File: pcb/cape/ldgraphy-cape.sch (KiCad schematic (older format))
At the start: 22 parts, among them P1 12V, P2 Laser, P3 Jumper, P4 Stepper, P5 CONN_01X05, P6 12V-in, P7 5V-in, P8 BB_P8, P9 BB_P9, Q1 BC237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

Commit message: o Update cape: include hsync circuit o Laser driver: new board that uses the new OpAmp circuit   (not tested yet)
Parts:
- removed C1: 100n, Capacitors_SMD:C_0805, symbol C
- removed C2: 10u, Capacitors_SMD:C_1206, symbol C
- removed P1: 12V, Pin_Headers:Pin_Header_Straight_1x02, symbol CONN_01X02
- removed P4: Stepper, Pin_Headers:Pin_Header_Straight_1x04, symbol CONN_01X04
- removed Q1: BC237, TO_SOT_Packages_THT:TO-92_Molded_Narrow_Reverse, symbol BC237
- removed Q2: BD135, TO_SOT_Packages_THT:SOT126_SOT32_Housing_Horizontal, symbol BD135
- removed Q3: MTM232270, TO_SOT_Packages_SMD:SOT-323, symbol Q_NMOS_GSD
- removed R1: R, Resistors_ThroughHole:Resistor_Horizontal_RM15mm, symbol R
- removed R2, R3: R, Capacitors_SMD:C_0603, symbol R
- removed R4: 100, Resistors_SMD:R_0603, symbol R
- removed R5: 4R7, Resistors_ThroughHole:Resistor_Horizontal_RM15mm, symbol R
- removed R6: 470, Resistors_ThroughHole:Resistor_Horizontal_RM15mm, symbol R
- removed RV1: POT, Potentiometers:Potentiometer_WirePads_Small, symbol POT
- added C10: C, Capacitors_SMD:C_0603, symbol C
- added P4: CONN_02X04, Pin_Headers:Pin_Header_Straight_2x04_Pitch2.54mm_SMD, symbol CONN_02X04
- added R10, R11, R13, R14, R15, R9: R, Resistors_SMD:R_0603, symbol R
- added R12: 1k, Resistors_SMD:R_0603, symbol R
- added R16: 2k2, Resistors_SMD:R_0603, symbol R
- added TP4: HSync, Measurement_Points:Measurement_Point_Round-SMD-Pad_Small, symbol TEST_1P
- added TP5: VPhoto, Measurement_Points:Measurement_Point_Round-SMD-Pad_Small, symbol TEST_1P
- added U3, U4: MIC920, TO_SOT_Packages_SMD:SOT-353_SC-70-5, symbol MIC920
- P2: value Laser -> PhDiode; footprint Pin_Headers:Pin_Header_Straight_1x02 -> Pin_Headers:Pin_Header_Straight_2x01_Pitch2.54mm
- P3: footprint (none) -> Pin_Headers:Pin_Header_Straight_2x03_Pitch2.54mm_SMD
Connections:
- net labels added: HSyncTrig, Hsync, VPhoto, ~MOTORS_EN
- net labels removed: ~SLED_EN
- wire segments 56 -> 66
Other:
- note added: "A"
- note added: "K"
- note added: "Photo Diode Amp"
- note added: "Schmitt Trigger"
- note removed: "Keep laser lasing at\nlow level when "off"."
- note removed: "≈1.2V"
- note removed: "≈1.9V"
- moved on the sheet: P3, P5, P6, P7, U1

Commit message: o Sketch out cape. NB: different GPIO assignment than   current software expects.
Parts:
- removed P8: BB_P8, Pin_Headers:Pin_Header_Straight_2x23, symbol CONN_02X32
- added J1: CONN_01X03, Pin_Headers:Pin_Header_Straight_1x03_Pitch2.54mm, symbol CONN_01X03
- added R1: 4k7, Resistors_SMD:R_0603, symbol R
- added R2, R3, R4: 1k, Resistors_SMD:R_0603, symbol R
- P4: value CONN_02X04 -> BaseConn; footprint Pin_Headers:Pin_Header_Straight_2x04_Pitch2.54mm_SMD -> Pin_Headers:Pin_Header_Straight_2x05_Pitch2.54mm_SMD; symbol CONN_02X04 -> CONN_02X05
- P9: footprint Pin_Headers:Pin_Header_Straight_2x23 -> Pin_Headers:Pin_Header_Straight_2x18_Pitch2.54mm; symbol CONN_02X32 -> CONN_02X23
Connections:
- net +12V: now also J1.1 (P1)
- net 3.3V: now also R1.1, R2.2, R3.2, R4.2
- net GND: now also P4.5 (P5), P4.6 (P6), J1.3 (P3); no longer P4.3 (P3), P4.4 (P4)
- net Hsync: now also P9.23 (P23), R12.1, R16.2; no longer P9.11 (P11)
- net LASER_DATA: now also J1.2 (P2)
- net SLED_DIR: now also P9.14 (P14); no longer P9.15 (P15)
- net SLED_STEP: now also P9.15 (P15); no longer P9.14 (P14)
- net ~MOTORS_EN: now also P9.16 (P16), R1.2; no longer P9.13 (P13)
- net ~StopBack: now reaches P9.12 (P12)
- net ~StopBack: now also P4.4 (P4), R4.1
- net at U1.11 (1B): now also P4.8 (P8); no longer P4.6 (P6)
- net at U1.12 (1A): now also P4.10 (P10); no longer P4.8 (P8)
- net at U1.13 (2A): now also P4.9 (P9); no longer P4.7 (P7)
- net at U1.14 (2B): now also P4.7 (P7); no longer P4.5 (P5)
- net ~UI-Button: now reaches P4.2 (P2)
- net ~UI-Button: now also P9.11 (P11), R3.1
- new net ~StopFront: P4.3 (P3), P9.13 (P13), R2.1

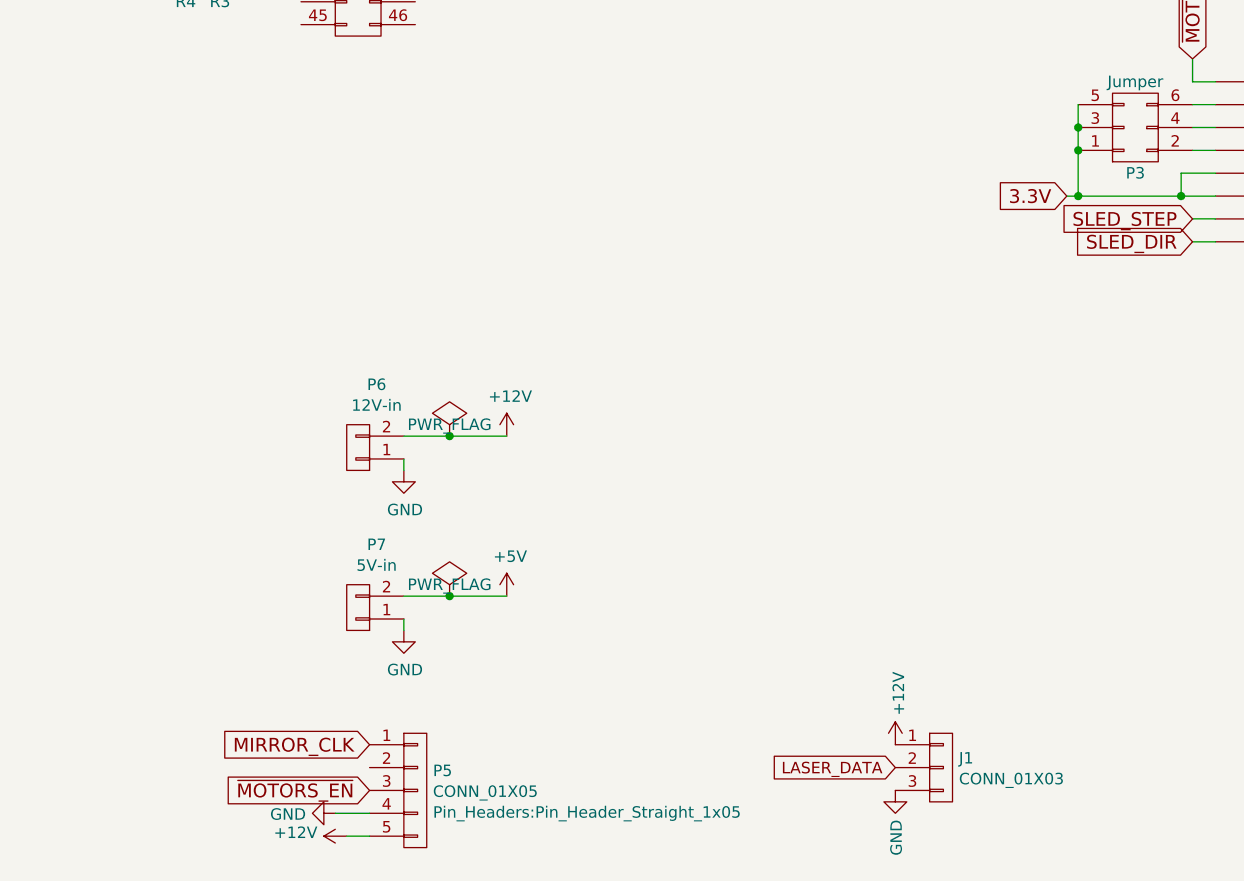
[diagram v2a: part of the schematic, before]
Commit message: o Add DC/DC converter to cape.
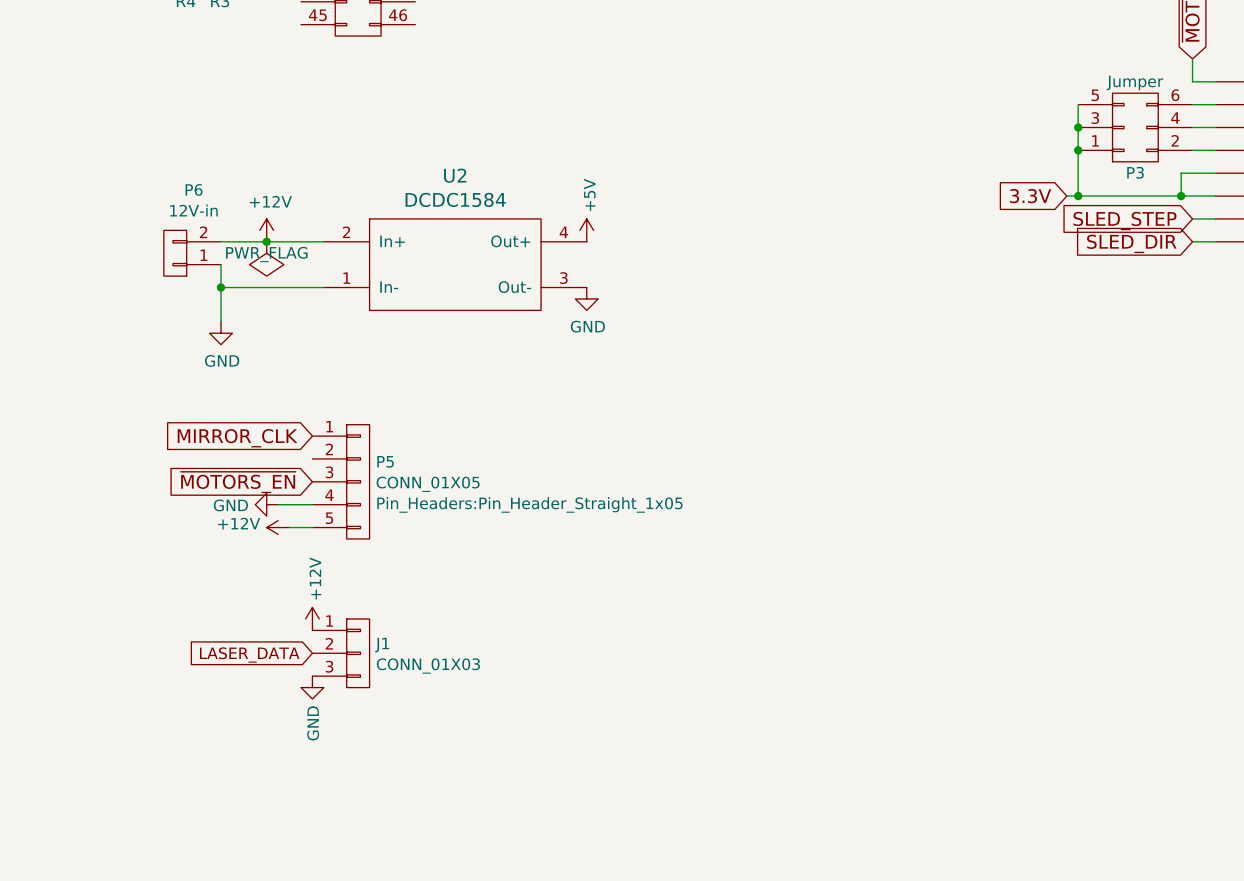
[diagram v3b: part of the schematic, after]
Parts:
- removed P7: 5V-in, symbol CONN_01X02
- added U2: DCDC1584, ldgraphy:dcdc-mp1584, symbol DCDC1584
- P6: footprint (none) -> Pin_Headers:Pin_Header_Straight_1x02_Pitch2.54mm
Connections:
- net +12V: now also U2.2 (In+)
- net +5V: now also U2.4 (Out+)
- net GND: now also U2.1 (In-), U2.3 (Out-)
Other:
- moved on the sheet: J1, P5, P6

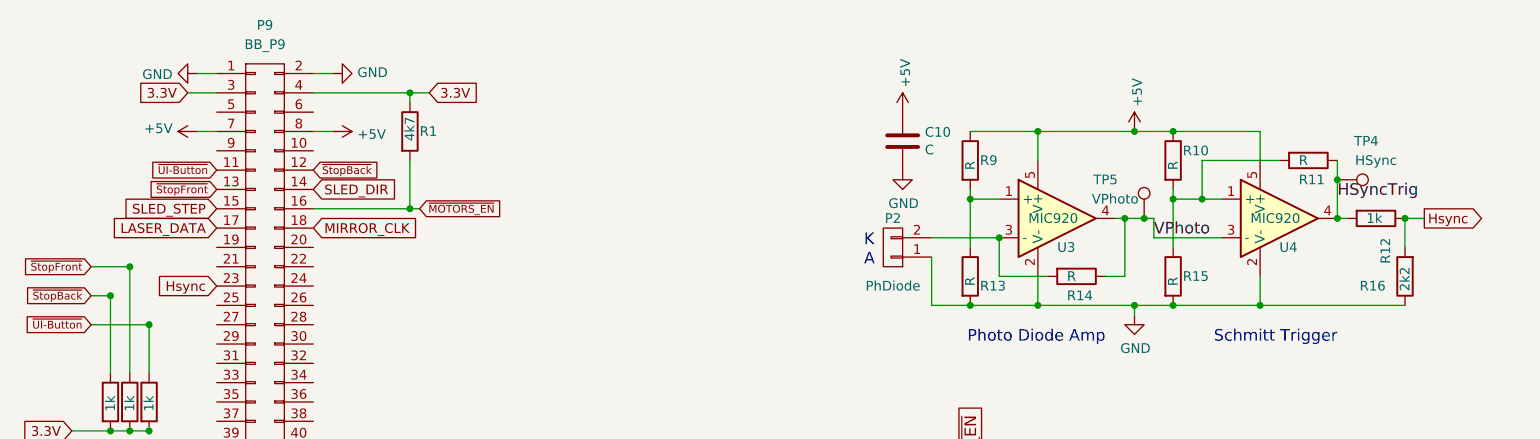
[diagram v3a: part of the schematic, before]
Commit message: o Update values in schematics.
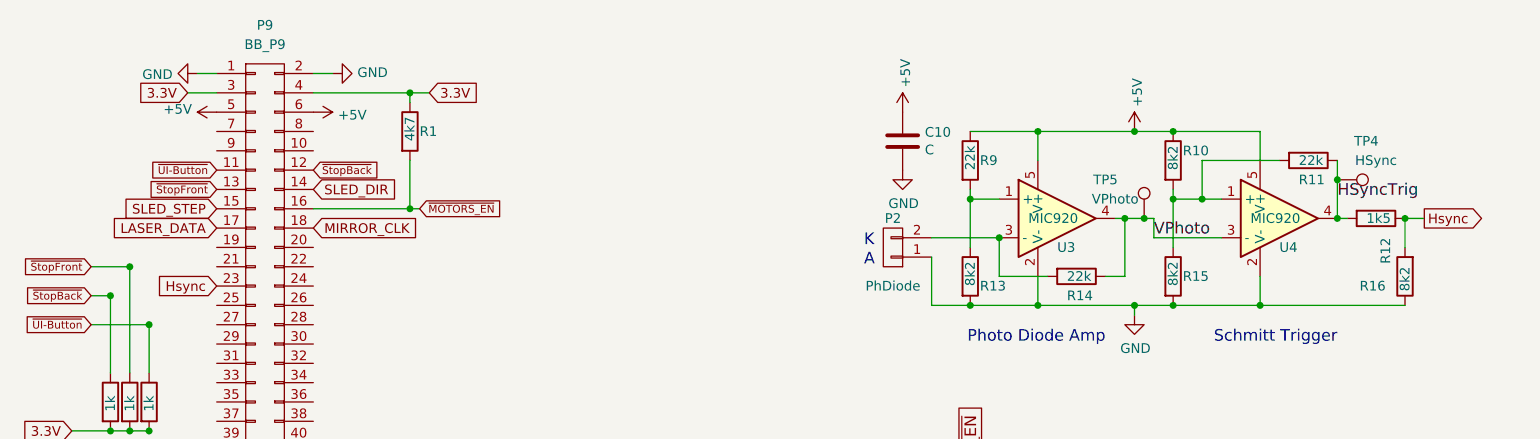
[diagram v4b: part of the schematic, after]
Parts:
- R10, R13, R15: value R -> 8k2
- R11, R14, R9: value R -> 22k
- R12: value 1k -> 1k5
- R16: value 2k2 -> 8k2
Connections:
- net +5V: now also P9.5 (P5), P9.6 (P6); no longer P9.7 (P7), P9.8 (P8)
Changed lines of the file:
@@
 L +5V #PWR5
 U 1 1 58741152
-P 2400 1350
-F 0 "#PWR5" H 2400 1200 50  0001 C CNN
-F 1 "+5V" V 2415 1478 50  0000 L CNN
-F 2 "" H 2400 1350 50  0000 C CNN
-F 3 "" H 2400 1350 50  0000 C CNN
-	1    2400 1350
+P 2300 1250
+F 0 "#PWR5" H 2300 1100 50  0001 C CNN
+F 1 "+5V" V 2315 1378 50  0000 L CNN
+F 2 "" H 2300 1250 50  0000 C CNN
+F 3 "" H 2300 1250 50  0000 C CNN
+	1    2300 1250
 	0    1    1    0
 $EndComp
@@
 L +5V #PWR4
 U 1 1 587412CA
-P 1700 1350
-F 0 "#PWR4" H 1700 1200 50  0001 C CNN
-F 1 "+5V" V 1715 1478 50  0000 L CNN
-F 2 "" H 1700 1350 50  0000 C CNN
-F 3 "" H 1700 1350 50  0000 C CNN
-	1    1700 1350
+P 1800 1250
+F 0 "#PWR4" H 1800 1100 50  0001 C CNN
+F 1 "+5V" V 1815 1378 50  0000 L CNN
+F 2 "" H 1800 1250 50  0000 C CNN
+F 3 "" H 1800 1250 50  0000 C CNN
+	1    1800 1250
 	0    -1   -1   0
 $EndComp
@@
 P 5700 1500
 F 0 "R9" H 5750 1500 50  0000 L CNN
-F 1 "R" V 5700 1450 50  0000 L CNN
+F 1 "22k" V 5700 1450 50  0000 L CNN
 F 2 "Resistors_SMD:R_0603" V 5630 1500 50  0001 C CNN
 F 3 "" H 5700 1500 50  0000 C CNN
@@
 P 5700 2100
 F 0 "R13" H 5750 2050 50  0000 L CNN
-F 1 "R" V 5700 2050 50  0000 L CNN
+F 1 "8k2" V 5700 2050 50  0000 L CNN
 F 2 "Resistors_SMD:R_0603" V 5630 2100 50  0001 C CNN
 F 3 "" H 5700 2100 50  0000 C CNN
@@
 P 6750 2100
 F 0 "R15" H 6800 2100 50  0000 L CNN
-F 1 "R" V 6750 2050 50  0000 L CNN
+F 1 "8k2" V 6750 2050 50  0000 L CNN
 F 2 "Resistors_SMD:R_0603" V 6680 2100 50  0001 C CNN
 F 3 "" H 6750 2100 50  0000 C CNN
@@
 P 6750 1500
 F 0 "R10" H 6800 1550 50  0000 L CNN
-F 1 "R" V 6750 1450 50  0000 L CNN
+F 1 "8k2" V 6750 1450 50  0000 L CNN
 F 2 "Resistors_SMD:R_0603" V 6680 1500 50  0001 C CNN
 F 3 "" H 6750 1500 50  0000 C CNN
@@
 P 7450 1500
 F 0 "R11" V 7550 1450 50  0000 L CNN
-F 1 "R" V 7450 1450 50  0000 L CNN
+F 1 "22k" V 7450 1450 50  0000 L CNN
 F 2 "Resistors_SMD:R_0603" V 7380 1500 50  0001 C CNN
 F 3 "" H 7450 1500 50  0000 C CNN
@@
 P 6250 2100
 F 0 "R14" V 6350 2050 50  0000 L CNN
-F 1 "R" V 6250 2050 50  0000 L CNN
+F 1 "22k" V 6250 2050 50  0000 L CNN
 F 2 "Resistors_SMD:R_0603" V 6180 2100 50  0001 C CNN
 F 3 "" H 6250 2100 50  0000 C CNN
@@
 P 7800 1800
 F 0 "R12" H 7900 1850 50  0000 L CNN
-F 1 "1k" V 7800 1750 50  0000 L CNN
+F 1 "1k5" V 7800 1750 50  0000 L CNN
 F 2 "Resistors_SMD:R_0603" V 7730 1800 50  0001 C CNN
 F 3 "" H 7800 1800 50  0000 C CNN
@@
 P 7950 2100
 F 0 "R16" H 8050 2150 50  0000 L CNN
-F 1 "2k2" V 7950 2050 50  0000 L CNN
+F 1 "8k2" V 7950 2050 50  0000 L CNN
 F 2 "Resistors_SMD:R_0603" V 7880 2100 50  0001 C CNN
 F 3 "" H 7950 2100 50  0000 C CNN
@@
 Connection ~ 1650 4200
 Wire Wire Line
-	2300 1350 2400 1350
-Wire Wire Line
-	1700 1350 1800 1350
-Wire Wire Line
 	7700 3700 7700 3450
